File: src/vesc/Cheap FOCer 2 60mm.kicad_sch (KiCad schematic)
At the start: 49 parts, among them J1 Conn_01x02, J2 Conn_01x07, J3 Conn_01x03, J6 Conn_01x03, P1 MOTOR1, P2 MOTOR1, P3 MOTOR1, P4 HALL/Encoder

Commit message: remove IMU and servo from schematic
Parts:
- removed C4: .01uF, Capacitor_SMD:C_0603_1608Metric, symbol BLDC_4-rescue:C-RESCUE-BLDC_4
- removed J3: Conn_01x03, Connector_JST:JST_PH_B3B-PH-K_1x03_P2.00mm_Vertical, symbol Connector_Generic:Conn_01x03
- removed R6: 100R, Resistor_SMD:R_0603_1608Metric, symbol BLDC_4-rescue:R-RESCUE-BLDC_4
- added P6: USB_C_Plug_USB2.0, symbol Connector:USB_C_Plug_USB2.0
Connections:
- net GND: now also P6.A1 (GND), P6.A12 (GND), P6.B1 (GND), P6.B12 (GND), P6.S1 (SHIELD)
- net at USB1.2 (D-): no longer R4.2
- net at USB1.3 (D+): no longer R3.2
- new net: P6.A7 (D-), R4.2
- new net: P6.A6 (D+), R3.2
- new net: P6.A4 (VBUS), P6.A9 (VBUS), P6.B4 (VBUS), P6.B9 (VBUS)
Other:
- removed sheet IMU

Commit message: Change SWD header to meet spec and add XT30 connector (schematic)
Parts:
- removed H7: MountingHole, MountingHole:MountingHole_3.2mm_M3_ISO14580_Pad, symbol Mechanical:MountingHole_Pad
- removed POS1: POS, CRF1:1pin_4mm, symbol BLDC_4-rescue:CONN_1
- removed USB1: USB Micro U-D-M5DD-W-1, Connector_USB:USB_Micro-B_Wuerth_614105150721_Vertical, symbol Connector:USB_B_Micro
- added J3: Conn_01x02, symbol Connector_Generic:Conn_01x02
- R1: value 39k -> 47k
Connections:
- net GND: now also J3.2 (Pin_2)
- net V_SUPPLY: now also J3.1 (Pin_1)
- no-connect marks 2 -> 0
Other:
- moved on the sheet: NEG3

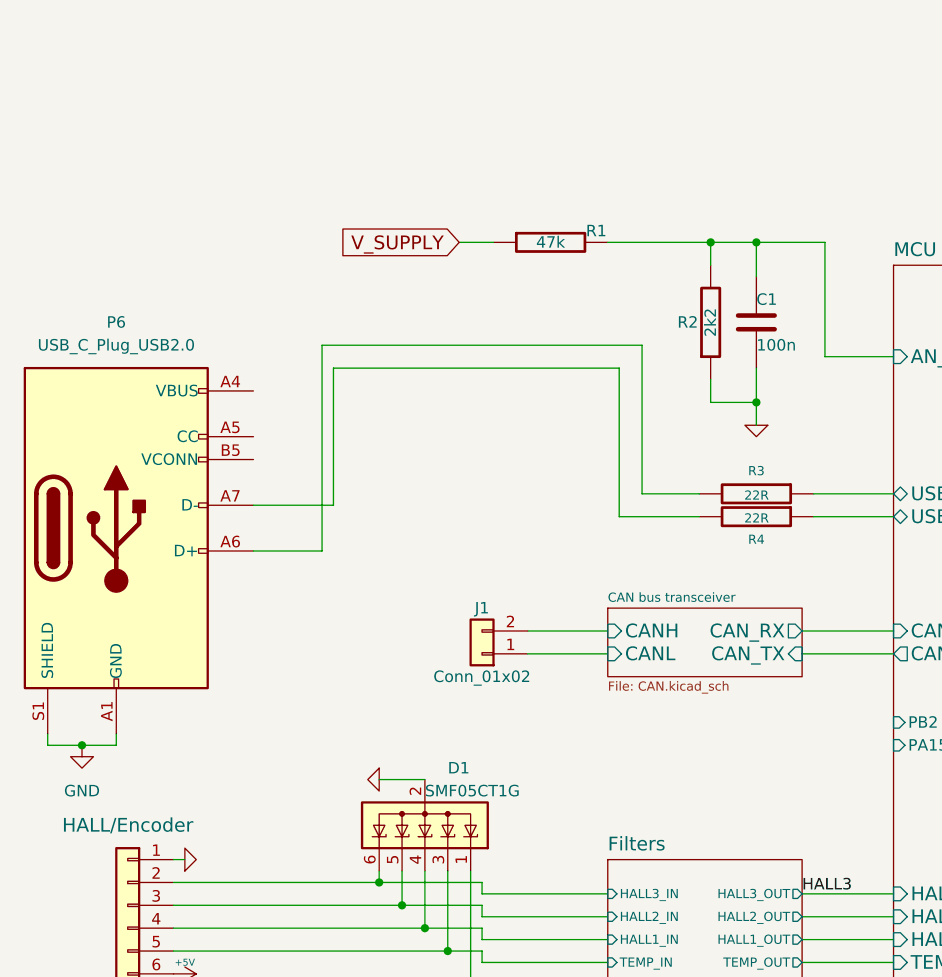
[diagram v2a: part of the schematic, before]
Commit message: Changed voltage divider resistor values
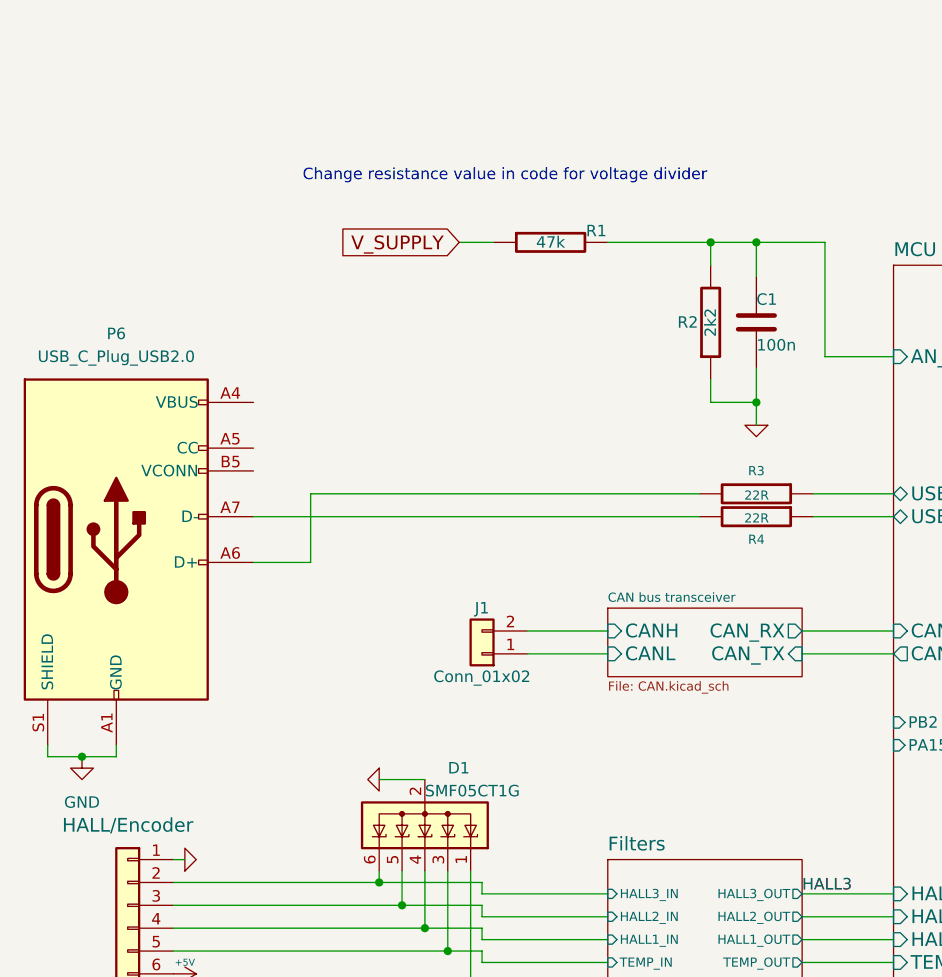
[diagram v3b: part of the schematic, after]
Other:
- note added: "Change resistance value in code for voltage divider"
- moved on the sheet: P6
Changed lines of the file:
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@@
 		)
 	)
+	(text "Change resistance value in code for voltage divider"
+		(exclude_from_sim no)
+		(at 118.11 85.344 0)
+		(effects
+			(font
+				(size 1.27 1.27)
+			)
+		)
+	)
 	(text "Voltage supply (0 - 51v)"
 		(exclude_from_sim no)
@@
 	)
 	(junction
-		(at 71.12 148.59)
+		(at 71.12 149.86)
 		(diameter 0)
 		(color 0 0 0 0)
@@
 	(wire
 		(pts
-			(xy 67.31 148.59) (xy 71.12 148.59)
+			(xy 67.31 149.86) (xy 71.12 149.86)
 		)
 		(stroke
@@
 	(wire
 		(pts
-			(xy 74.93 147.32) (xy 74.93 148.59)
+			(xy 74.93 148.59) (xy 74.93 149.86)
 		)
 		(stroke
@@
 	(wire
 		(pts
-			(xy 133.35 120.65) (xy 133.35 104.14)
-		)
-		(stroke
-			(width 0)
-			(type default)
-		)
-	)
-	(wire
-		(pts
 			(xy 128.27 196.85) (xy 128.27 195.58)
 		)
@@
 		)
 	)
-	(wire
-		(pts
-			(xy 130.81 106.68) (xy 99.06 106.68)
-		)
-		(stroke
-			(width 0)
-			(type default)
-		)
-	)
 	(polyline
 		(pts
@@
 	(wire
 		(pts
-			(xy 139.7 120.65) (xy 133.35 120.65)
-		)
-		(stroke
-			(width 0)
-			(type default)
-		)
-	)
-	(wire
-		(pts
 			(xy 151.13 165.1) (xy 161.29 165.1)
 		)
@@
 	(wire
 		(pts
-			(xy 99.06 121.92) (xy 90.17 121.92)
+			(xy 90.17 123.19) (xy 139.7 123.19)
 		)
 		(stroke
@@
 	(wire
 		(pts
-			(xy 130.81 123.19) (xy 130.81 106.68)
-		)
-		(stroke
-			(width 0)
-			(type default)
-		)
-	)
-	(wire
-		(pts
 			(xy 335.28 123.19) (xy 334.01 123.19)
 		)
@@
 		)
 	)
-	(wire
-		(pts
-			(xy 139.7 123.19) (xy 130.81 123.19)
-		)
-		(stroke
-			(width 0)
-			(type default)
-		)
-	)
 	(polyline
 		(pts
@@
 	(wire
 		(pts
-			(xy 74.93 148.59) (xy 71.12 148.59)
+			(xy 74.93 149.86) (xy 71.12 149.86)
 		)
 		(stroke
@@
 	(wire
 		(pts
-			(xy 90.17 127) (xy 97.79 127)
+			(xy 90.17 128.27) (xy 96.52 128.27)
 		)
 		(stroke
@@
 	(wire
 		(pts
-			(xy 97.79 104.14) (xy 97.79 127)
+			(xy 96.52 120.65) (xy 96.52 128.27)
 		)
 		(stroke
@@
 	(wire
 		(pts
-			(xy 99.06 106.68) (xy 99.06 121.92)
-		)
-		(stroke
-			(width 0)
-			(type default)
-		)
-	)
-	(wire
-		(pts
 			(xy 83.82 191.77) (xy 78.74 191.77)
 		)
@@
 	(wire
 		(pts
-			(xy 67.31 147.32) (xy 67.31 148.59)
+			(xy 67.31 148.59) (xy 67.31 149.86)
 		)
 		(stroke
@@
 	(wire
 		(pts
-			(xy 133.35 104.14) (xy 97.79 104.14)
+			(xy 96.52 120.65) (xy 139.7 120.65)
 		)
 		(stroke
@@
 	(symbol
 		(lib_id "power:GND")
-		(at 71.12 148.59 0)
+		(at 71.12 149.86 0)
 		(unit 1)
 		(exclude_from_sim no)
@@
 		(fields_autoplaced yes)
 		(property "Reference" "#PWR015"
-			(at 71.12 154.94 0)
+			(at 71.12 156.21 0)
 			(effects
 				(font
@@
 		)
 		(property "Value" "GND"
-			(at 71.12 153.67 0)
+			(at 71.12 154.94 0)
 			(effects
 				(font
@@
 		)
 		(property "Footprint" ""
-			(at 71.12 148.59 0)
+			(at 71.12 149.86 0)
 			(effects
 				(font
@@
 		)
 		(property "Datasheet" ""
-			(at 71.12 148.59 0)
+			(at 71.12 149.86 0)
 			(effects
 				(font
@@
 		)
 		(property "Description" "Power symbol creates a global label with name \"GND\" , ground"
-			(at 71.12 148.59 0)
+			(at 71.12 149.86 0)
 			(effects
 				(font
@@
 	(symbol
 		(lib_id "Connector:USB_C_Plug_USB2.0")
-		(at 74.93 124.46 0)
+		(at 74.93 125.73 0)
 		(unit 1)
 		(exclude_from_sim no)
@@
 		(fields_autoplaced yes)
 		(property "Reference" "P6"
-			(at 74.93 101.6 0)
+			(at 74.93 102.87 0)
 			(effects
 				(font
@@
 		)
 		(property "Value" "USB_C_Plug_USB2.0"
-			(at 74.93 104.14 0)
+			(at 74.93 105.41 0)
 			(effects
 				(font
@@
 		)
 		(property "Footprint" ""
-			(at 78.74 124.46 0)
+			(at 78.74 125.73 0)
 			(effects
 				(font
@@
 		)
 		(property "Datasheet" "https://www.usb.org/sites/default/files/documents/usb_type-c.zip"
-			(at 78.74 124.46 0)
+			(at 78.74 125.73 0)
 			(effects
 				(font
@@
 		)
 		(property "Description" "USB 2.0-only Type-C Plug connector"
-			(at 74.93 124.46 0)
+			(at 74.93 125.73 0)
 			(effects
 				(font

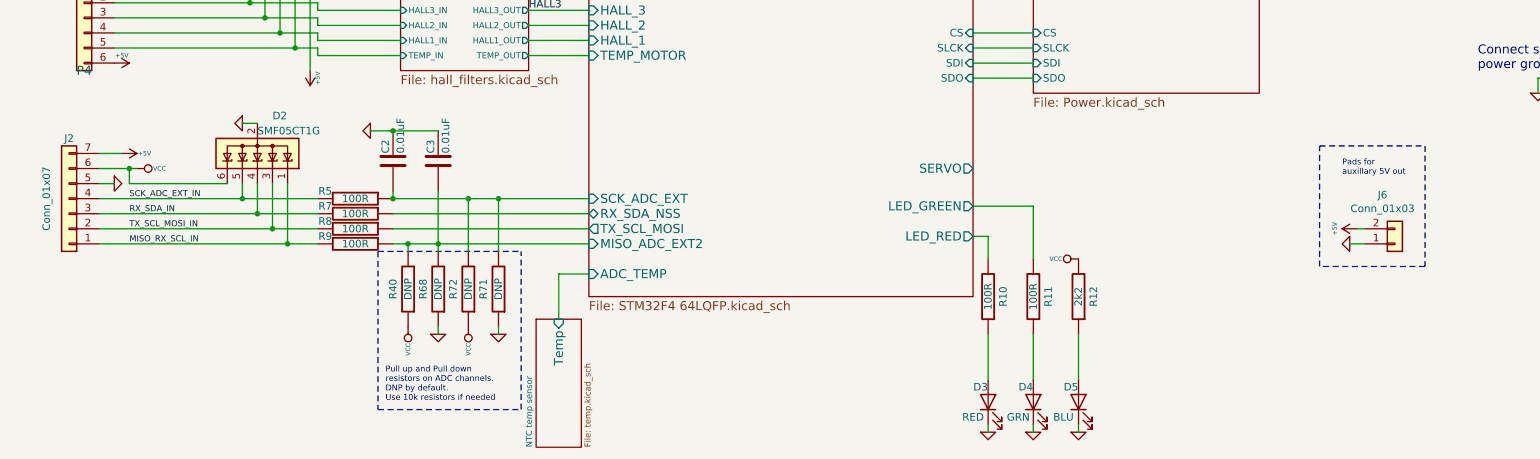
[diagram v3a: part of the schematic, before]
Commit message: removed unused connectors
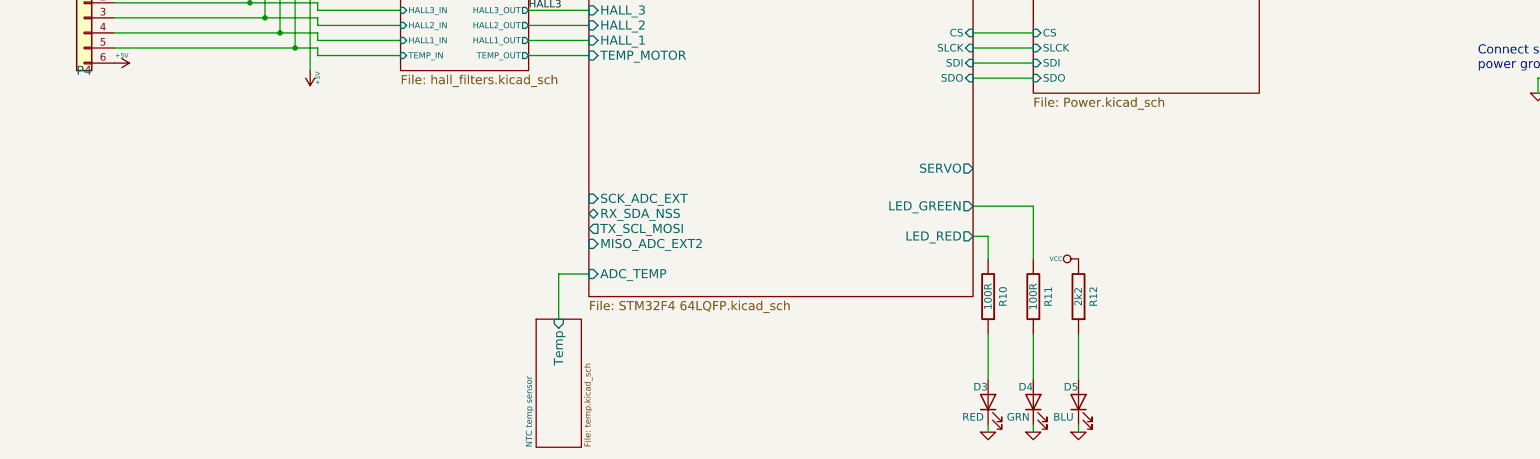
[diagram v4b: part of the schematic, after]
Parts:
- removed C2, C3: 0.01uF, Capacitor_SMD:C_0603_1608Metric, symbol BLDC_4-rescue:C-RESCUE-BLDC_4
- removed D2: SMF05CT1G, Package_TO_SOT_SMD:SOT-363_SC-70-6, symbol Power_Protection:SP0505BAHT
- removed J2: Conn_01x07, Connector_JST:JST_PH_B7B-PH-K_1x07_P2.00mm_Vertical, symbol Connector_Generic:Conn_01x07
- removed J6: Conn_01x03, Connector_PinHeader_2.54mm:PinHeader_1x02_P2.54mm_Vertical, symbol Connector_Generic:Conn_01x02
- removed R40, R68, R71, R72: DNP, Resistor_SMD:R_0603_1608Metric, symbol BLDC_4-rescue:R-RESCUE-BLDC_4
- removed R5, R7, R8, R9: 100R, Resistor_SMD:R_0603_1608Metric, symbol BLDC_4-rescue:R-RESCUE-BLDC_4
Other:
- note removed: "Pads for auxillary 5V out"
- note removed: "Pull up and Pull down resistors on ADC channels. DNP by default. Use 10k resistors if needed"

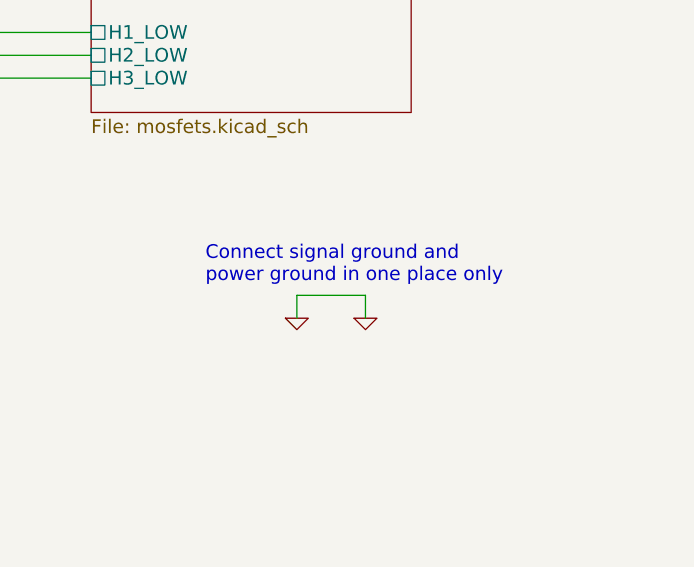
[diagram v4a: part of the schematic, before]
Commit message: removed signal and power ground connection
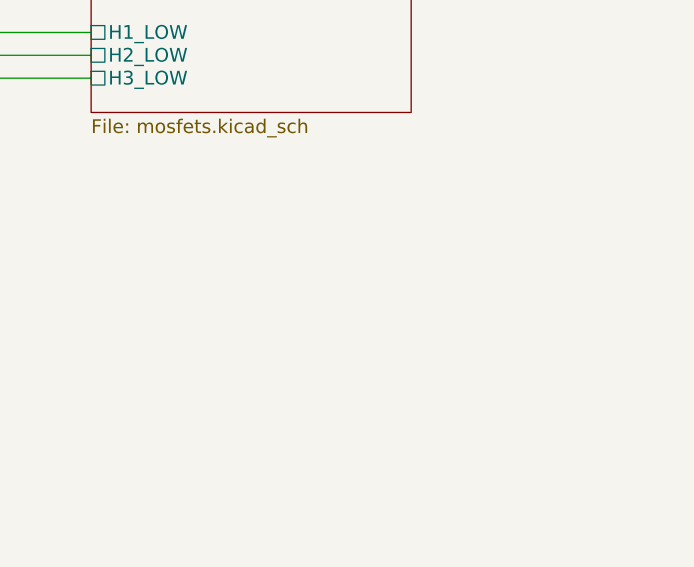
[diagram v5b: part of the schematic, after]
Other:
- note removed: "Connect signal ground and power ground in one place only"
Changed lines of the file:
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@@
-		)
-	)
-	(text "Connect signal ground and\npower ground in one place only"
-		(exclude_from_sim no)
-		(at 311.15 175.26 0)
-		(effects
-			(font
-				(size 1.524 1.524)
-			)
-			(justify left bottom)
 		)
 	)
@@
 	(wire
 		(pts
-			(xy 328.93 176.53) (xy 328.93 179.07)
-		)
-		(stroke
-			(width 0)
-			(type default)
-		)
-	)
-	(wire
-		(pts
 			(xy 309.88 87.63) (xy 303.53 87.63)
 		)
@@
 		)
 	)
-	(wire
-		(pts
-			(xy 321.31 176.53) (xy 321.31 179.07)
-		)
-		(stroke
-			(width 0)
-			(type default)
-		)
-	)
 	(polyline
 		(pts
@@
 		(pts
 			(xy 81.28 161.29) (xy 82.55 161.29)
-		)
-		(stroke
-			(width 0)
-			(type default)
-		)
-	)
-	(wire
-		(pts
-			(xy 321.31 176.53) (xy 328.93 176.53)
 		)
 		(stroke
@@
 	)
 	(symbol
-		(lib_id "BLDC_4-rescue:GND-RESCUE-BLDC_4")
-		(at 321.31 179.07 0)
-		(unit 1)
-		(exclude_from_sim no)
-		(in_bom yes)
-		(on_board yes)
-		(dnp no)
-		(property "Reference" "#PWR09"
-			(at 321.31 179.07 0)
-			(effects
-				(font
-					(size 0.762 0.762)
-				)
-				(hide yes)
-			)
-		)
-		(property "Value" "GND"
-			(at 321.31 180.848 0)
-			(effects
-				(font
-					(size 0.762 0.762)
-				)
-				(hide yes)
-			)
-		)
-		(property "Footprint" ""
-			(at 321.31 179.07 0)
-			(effects
-				(font
-					(size 1.524 1.524)
-				)
-				(hide yes)
-			)
-		)
-		(property "Datasheet" ""
-			(at 321.31 179.07 0)
-			(effects
-				(font
-					(size 1.524 1.524)
-				)
-				(hide yes)
-			)
-		)
-		(property "Description" ""
-			(at 321.31 179.07 0)
-			(effects
-				(font
-					(size 1.27 1.27)
-				)
-			)
-		)
-		(pin "1"
-		)
-		(instances
-			(project ""
-				(path "/8b53313b-c20e-4d2c-aeda-56c30dbca1c0"
-					(reference "#PWR09")
-					(unit 1)
-				)
-			)
-		)
-	)
-	(symbol
 		(lib_id "BLDC_4-rescue:R-RESCUE-BLDC_4")
 		(at 228.6 213.36 180)
@@
 					(unit 1)
 				)
-			)
-		)
-	)
-	(symbol
-		(lib_id "BLDC_4-rescue:GND-RESCUE-BLDC_4")
-		(at 328.93 179.07 0)
-		(unit 1)
-		(exclude_from_sim no)
-		(in_bom yes)
-		(on_board yes)
-		(dnp no)
-		(property "Reference" "#PWR010"
-			(at 328.93 179.07 0)
-			(effects
-				(font
-					(size 0.762 0.762)
-				)
-				(hide yes)
-			)
-		)
-		(property "Value" "GND"
-			(at 328.93 180.848 0)
-			(effects
-				(font
-					(size 0.762 0.762)
-				)
-				(hide yes)
-			)
-		)
-		(property "Footprint" ""
-			(at 328.93 179.07 0)
-			(effects
-				(font
-					(size 1.524 1.524)
-				)
-				(hide yes)
-			)
-		)
-		(property "Datasheet" ""
-			(at 328.93 179.07 0)
-			(effects
-				(font
-					(size 1.524 1.524)
-				)
-				(hide yes)
-			)
-		)
-		(property "Description" ""
-			(at 328.93 179.07 0)
-			(effects
-				(font
-					(size 1.27 1.27)
-				)
-			)
-		)
-		(pin "1"
-		)
-		(instances
-			(project ""
-				(path "/8b53313b-c20e-4d2c-aeda-56c30dbca1c0"
-					(reference "#PWR010")
-					(unit 1)
-				)

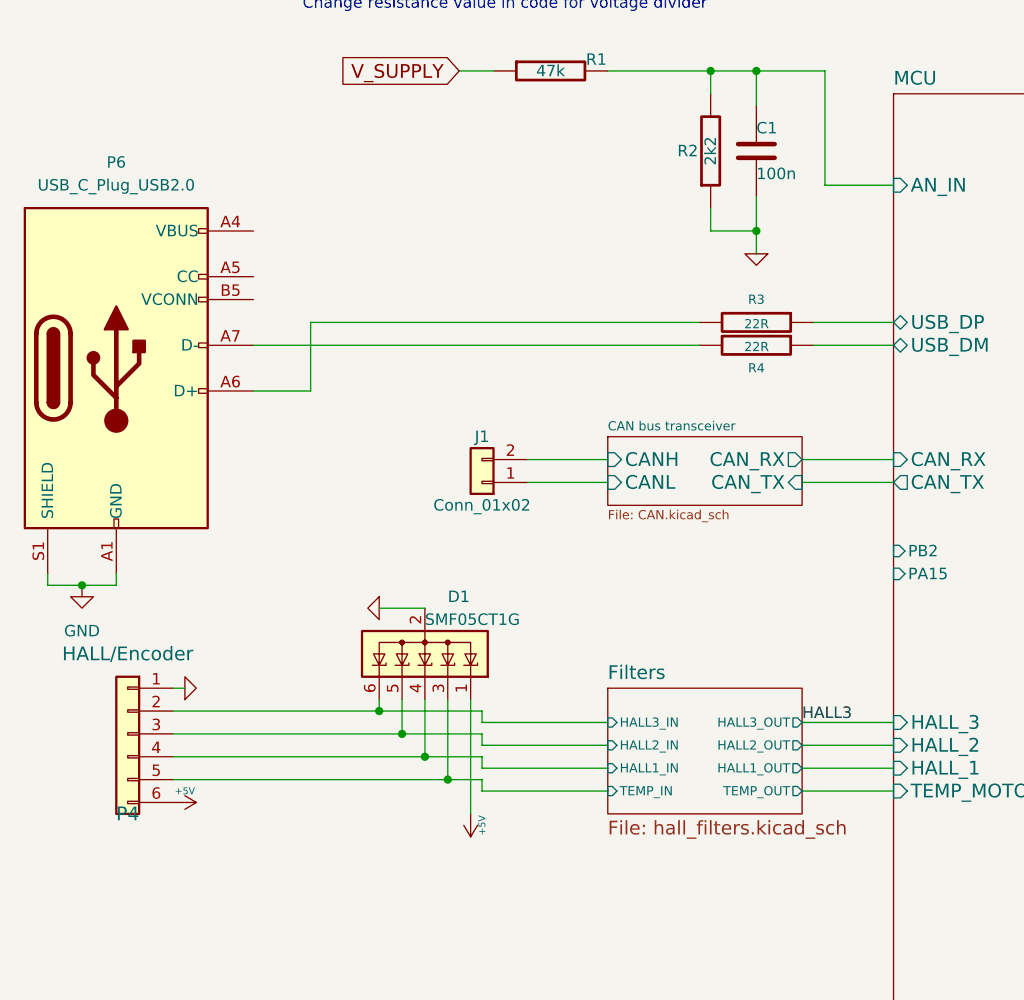
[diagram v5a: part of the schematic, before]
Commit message: std quad TVS diode for hall sensor
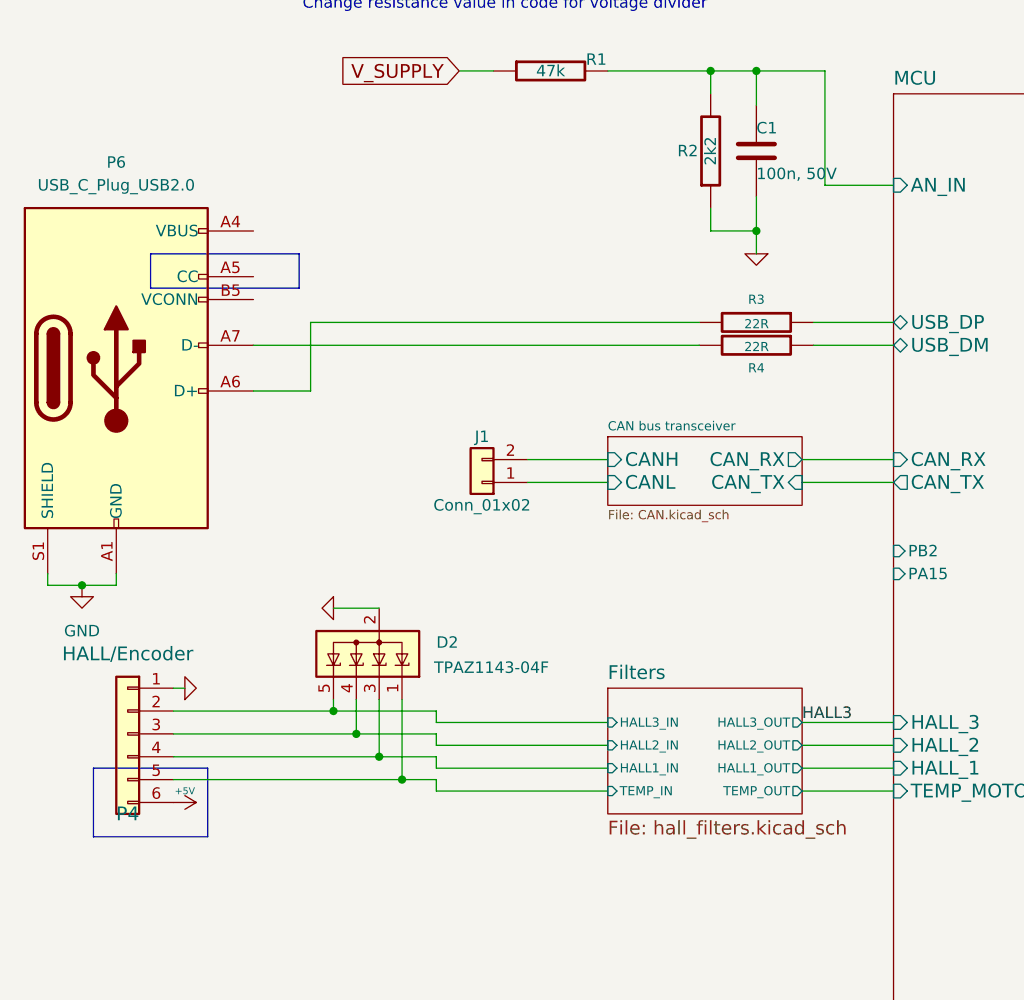
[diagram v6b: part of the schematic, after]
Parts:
- removed D1: SMF05CT1G, Package_TO_SOT_SMD:SOT-363_SC-70-6, symbol Power_Protection:SP0505BAHT
- added D2: TPAZ1143-04F, Package_TO_SOT_SMD:SOT-23-5, symbol Power_Protection:ESDA5V3SC5
- C1: value 100n -> 100n, 50V
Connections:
- net Filters/HALL1_IN: now also D2.3 (K)
- net Filters/HALL2_IN: now also D2.4 (K)
- net Filters/HALL3_IN: now also D2.5 (K)
- net Filters/TEMP_IN: now also D2.1 (K)
- net GND: now also D2.2 (A)
